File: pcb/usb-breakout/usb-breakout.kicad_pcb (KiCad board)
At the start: 2 copper layers, 20 x 20 mm, 7 parts, among them CN1 S7B-ZR-SM4A-TF(LF)(SN)_C51187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

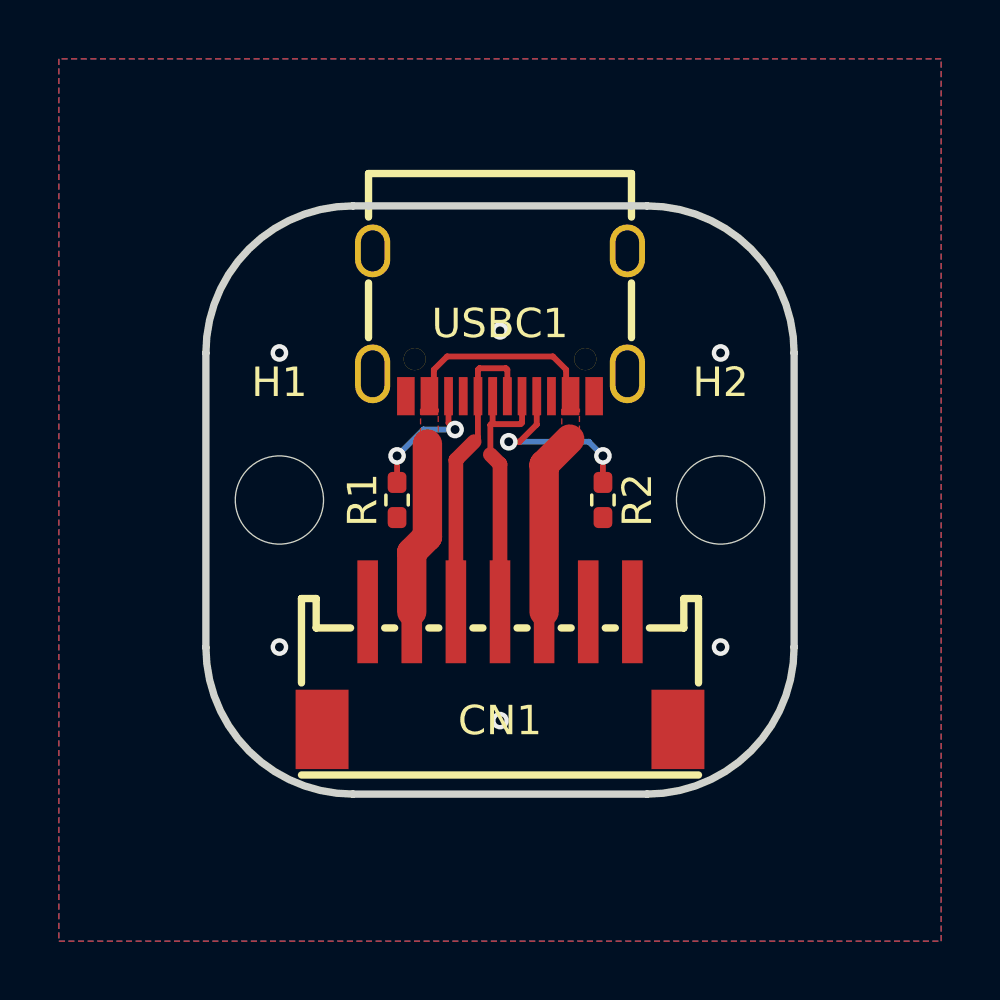
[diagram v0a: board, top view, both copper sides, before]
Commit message: NG | Update usb ext pinout, cleanup
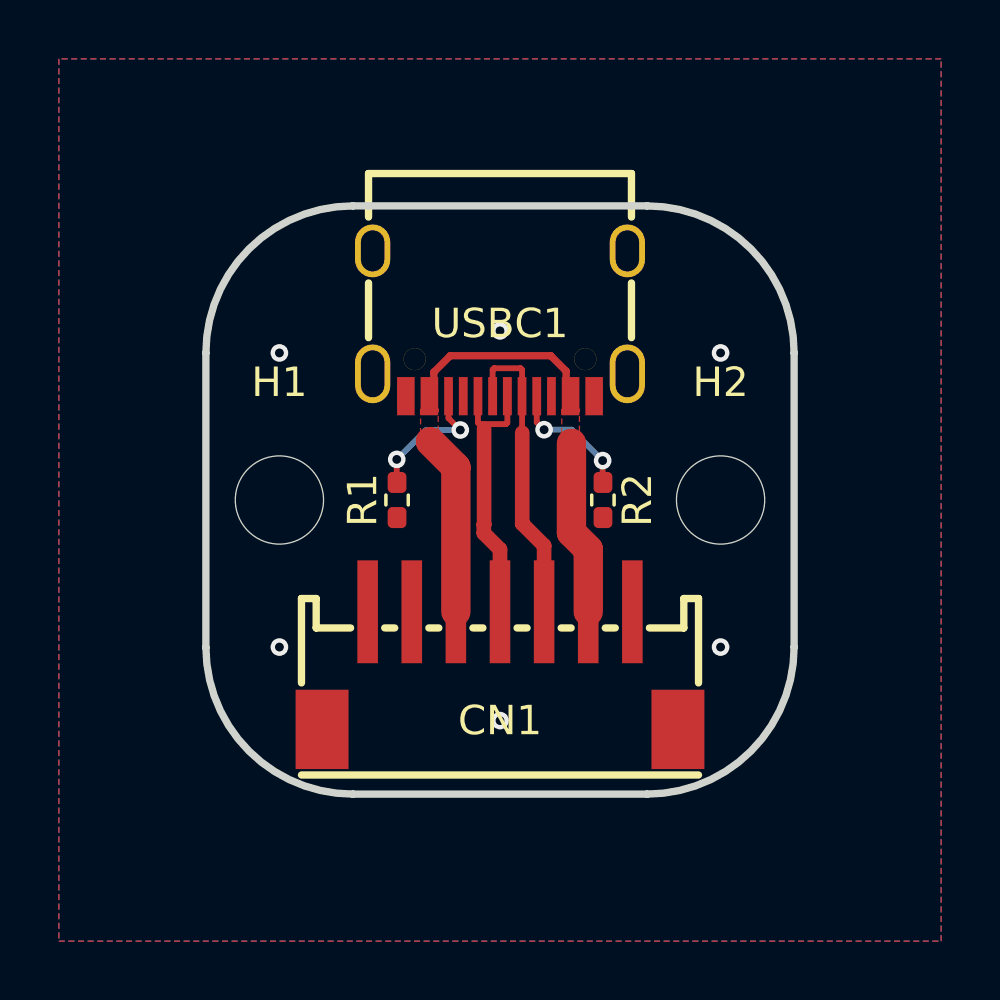
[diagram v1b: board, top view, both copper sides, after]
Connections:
- CN1 pad 2: +5V -> GND
- CN1 pad 3: D+ -> +5V
- CN1 pad 4: D- -> D+
- CN1 pad 5: +5V -> D-
- CN1 pad 6: GND -> +5V
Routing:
- net Net-(USBC1-CC1): track 6.47 -> 4.42 mm
- net D-: track 9.44 -> 10.5 mm
- net D+: track 10.3 -> 9.30 mm

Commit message: NG | Splitfox PCB Placement
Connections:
- CN1 pad 8: unconnected-(CN1-Pad8) -> GND
- CN1 pad 9: unconnected-(CN1-Pad9) -> GND
- USBC1 pad 0: unconnected-(USBC1-SH-Pad0) -> GND
- USBC1 pad 1: unconnected-(USBC1-SH-Pad1) -> GND
- USBC1 pad 2: unconnected-(USBC1-SH-Pad2) -> GND
- USBC1 pad 3: unconnected-(USBC1-SH-Pad3) -> GND
